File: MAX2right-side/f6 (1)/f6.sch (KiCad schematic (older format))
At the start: 72 parts, among them P1 CONN_02X10, P2 CONN_02X10, P3 170V, P4 dot, Q1 BC850, Q10 BC850, Q11 BC850, Q12 BC850, Q13 BC850, Q14 BC850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

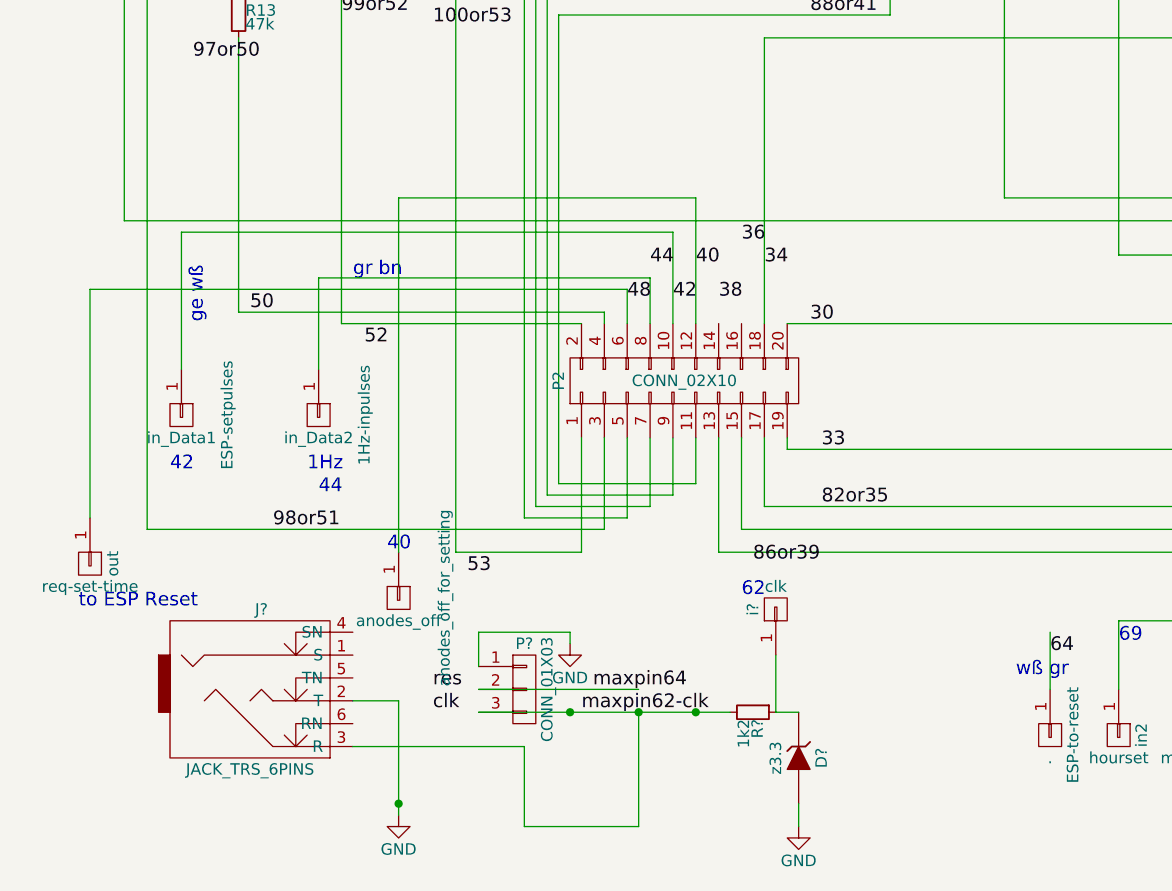
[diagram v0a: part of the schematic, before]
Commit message: 3x clk input
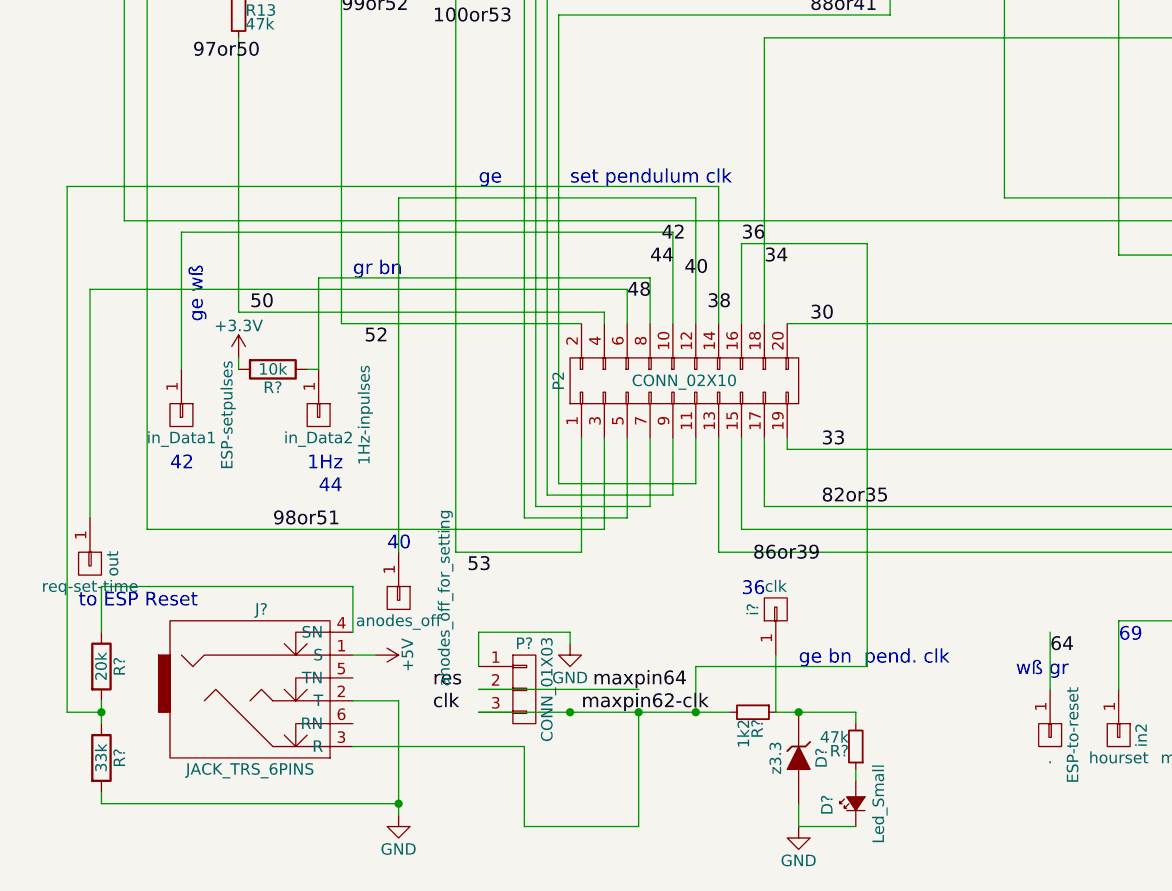
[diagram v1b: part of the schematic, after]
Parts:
- added D?: Led_Small, symbol Led_Small
- added R?: 20k, symbol R
- added R?: 33k, symbol R
- added R?: 47k, Resistors_SMD:R_0805, symbol R_Small
- added R?: 10k, symbol R
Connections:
- net maxpin62-clk is gone; now on net 36: J?.3 (R), P?.3 (P3), R?.2
- net +3V3: now also R?.2
- net +5V: now also J?.1 (S)
- net 36: now also P2.16 (P16)
- net 40: no longer P2.12 (P12), anodes_off_for_setting.1 (P1)
- net 42: no longer ESP-setpulses.1 (P1), P2.10 (P10)
- net GND: now also D?.1 (K), R?.2
- net at P2.14 (P14): now also R?.1, R?.2
- net at 1Hz-inpulses.1 (P1), P2.8 (P8): now also R?.1
- net at J?.4 (SN): now also R?.1
- net at D?.1 (K), R?.1, i?.1 (P1): now also R?.2
- new net: ESP-setpulses.1 (P1), P2.10 (P10)
- new net: P2.12 (P12), anodes_off_for_setting.1 (P1)
- new net: D?.2 (A), R?.1
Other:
- note added: "36"
- note added: "ge"
- note added: "ge bn pend. clk\n"
- note added: "set pendulum clk"
- note removed: "62"
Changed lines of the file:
@@
 Text Label 3050 5200 0    60   ~ 0
 44
-Text Label 3150 5350 0    60   ~ 0
+Text Label 3100 5100 0    60   ~ 0
 42
-Text Label 3250 5200 0    60   ~ 0
+Text Label 3200 5250 0    60   ~ 0
 40
-Text Label 3350 5350 0    60   ~ 0
+Text Label 3300 5400 0    60   ~ 0
 38
 Text Label 3450 5100 0    60   ~ 0
@@
 	3600 7150 3600 6900
 Wire Wire Line
-	3600 7150 3700 7150
+	3600 7150 3950 7150
 Wire Wire Line
 	3700 7550 3700 7650
@@
 40
 Text Notes 3450 6650 0    60   ~ 0
-62
+36
+$Comp
+L +5V #PWR?
+U 1 1 5AA94862
+P 1850 6900
+F 0 "#PWR?" H 1850 6750 50  0001 C CNN
+F 1 "+5V" H 1850 7040 50  0000 C CNN
+F 2 "" H 1850 6900 50  0000 C CNN
+F 3 "" H 1850 6900 50  0000 C CNN
+	1    1850 6900
+	0    1    1    0
+$EndComp
+Wire Wire Line
+	1850 6900 1750 6900
+$Comp
+L R R?
+U 1 1 5AA94D46
+P 650 6950
+F 0 "R?" V 730 6950 50  0000 C CNN
+F 1 "20k" V 650 6950 50  0000 C CNN
+F 2 "" V 580 6950 50  0000 C CNN
+F 3 "" H 650 6950 50  0000 C CNN
+	1    650  6950
+	1    0    0    -1
+$EndComp
+$Comp
+L R R?
+U 1 1 5AA94E40
+P 650 7350
+F 0 "R?" V 730 7350 50  0000 C CNN
+F 1 "33k" V 650 7350 50  0000 C CNN
+F 2 "" V 580 7350 50  0000 C CNN
+F 3 "" H 650 7350 50  0000 C CNN
+	1    650  7350
+	1    0    0    -1
+$EndComp
+Wire Wire Line
+	1750 6800 1750 6600
+Wire Wire Line
+	1750 6600 650  6600
+Wire Wire Line
+	650  6600 650  6800
+Wire Wire Line
+	650  7100 650  7200
+Wire Wire Line
+	650  7500 650  7550
+Wire Wire Line
+	650  7550 1950 7550
+Wire Wire Line
+	3350 5450 3350 4850
+Wire Wire Line
+	3350 4850 500  4850
+Wire Wire Line
+	500  4850 500  7150
+Wire Wire Line
+	500  7150 650  7150
+Connection ~ 650  7150
+Text Notes 2700 4850 0    60   ~ 0
+set pendulum clk
+Text Notes 2300 4850 0    60   ~ 0
+ge
+Wire Wire Line
+	3450 5450 3450 5100
+Wire Wire Line
+	3450 5100 4000 5100
+Wire Wire Line
+	4000 5100 4000 6950
+Wire Wire Line
+	4000 6950 3250 6950
+Wire Wire Line
+	3250 6950 3250 7150
+Text Notes 3700 6950 0    60   ~ 0
+ge bn  pend. clk\n
+$Comp
+L Led_Small D?
+U 1 1 5AA98C99
+P 3950 7550
+F 0 "D?" H 3900 7675 50  0000 L CNN
+F 1 "Led_Small" H 3775 7450 50  0000 L CNN
+F 2 "" V 3950 7550 50  0000 C CNN
+F 3 "" V 3950 7550 50  0000 C CNN
+	1    3950 7550
+	0    -1   -1   0
+$EndComp
+$Comp
+L R_Small R?
+U 1 1 5AA98DD3
+P 3950 7300
+F 0 "R?" H 3980 7320 50  0000 L CNN
+F 1 "47k" H 3980 7260 50  0000 L CNN
+F 2 "Resistors_SMD:R_0805" H 3950 7300 50  0001 C CNN
+F 3 "" H 3950 7300 50  0000 C CNN
+	1    3950 7300
+	-1   0    0    1
+$EndComp
+Wire Wire Line
+	3950 7400 3950 7450
+Wire Wire Line
+	3700 7650 3950 7650
+Wire Wire Line
+	3950 7150 3950 7200
+Connection ~ 3700 7150
+$Comp
+L R R?
+U 1 1 5AA9ED88
+P 1400 5650
+F 0 "R?" V 1480 5650 50  0000 C CNN
+F 1 "10k" V 1400 5650 50  0000 C CNN
+F 2 "" V 1330 5650 50  0000 C CNN
+F 3 "" H 1400 5650 50  0000 C CNN
+	1    1400 5650
+	0    1    1    0
+$EndComp
+Wire Wire Line
+	1250 5600 1250 5650
+Wire Wire Line
+	1600 5650 1550 5650
+$Comp
+L +3.3V #PWR?
+U 1 1 5AA9F331
+P 1250 5600
+F 0 "#PWR?" H 1250 5450 50  0001 C CNN
+F 1 "+3.3V" H 1250 5740 50  0000 C CNN
+F 2 "" H 1250 5600 50  0000 C CNN
+F 3 "" H 1250 5600 50  0000 C CNN
+	1    1250 5600
+	1    0    0    -1
+$EndComp
 $EndSCHEMATC

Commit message: added overview
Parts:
- anodes_off_for_setting: value anodes_off -> anodes_off A1
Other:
- note added: "gr rs"
- note added: "sw"
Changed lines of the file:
@@
 U 1 1 5A779E4F
 P 1950 6650
-F 0 "anodes_off_for_setting" H 1950 6850 50  0000 C CNN
-F 1 "anodes_off" V 2050 6650 50  0000 C CNN
+F 0 "anodes_off_for_setting" H 1200 6700 50  0000 C CNN
+F 1 "anodes_off A1" V 2050 6750 50  0000 C CNN
 F 2 "" H 1950 6650 50  0000 C CNN
 F 3 "" H 1950 6650 50  0000 C CNN
@@
 	1    0    0    -1
 $EndComp
+Text Notes 1950 6150 1    60   ~ 0
+gr rs
+Text Notes 5350 6750 2    60   ~ 0
+sw
+Text Notes 5650 6900 2    60   ~ 0
+wß
 $EndSCHEMATC
